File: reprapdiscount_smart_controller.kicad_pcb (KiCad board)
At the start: 2 copper layers, 150 x 55 mm, 38 parts, among them Q1 BC817, Q2 BC817, U1 74HC4050, U2 AMS1117-3.3

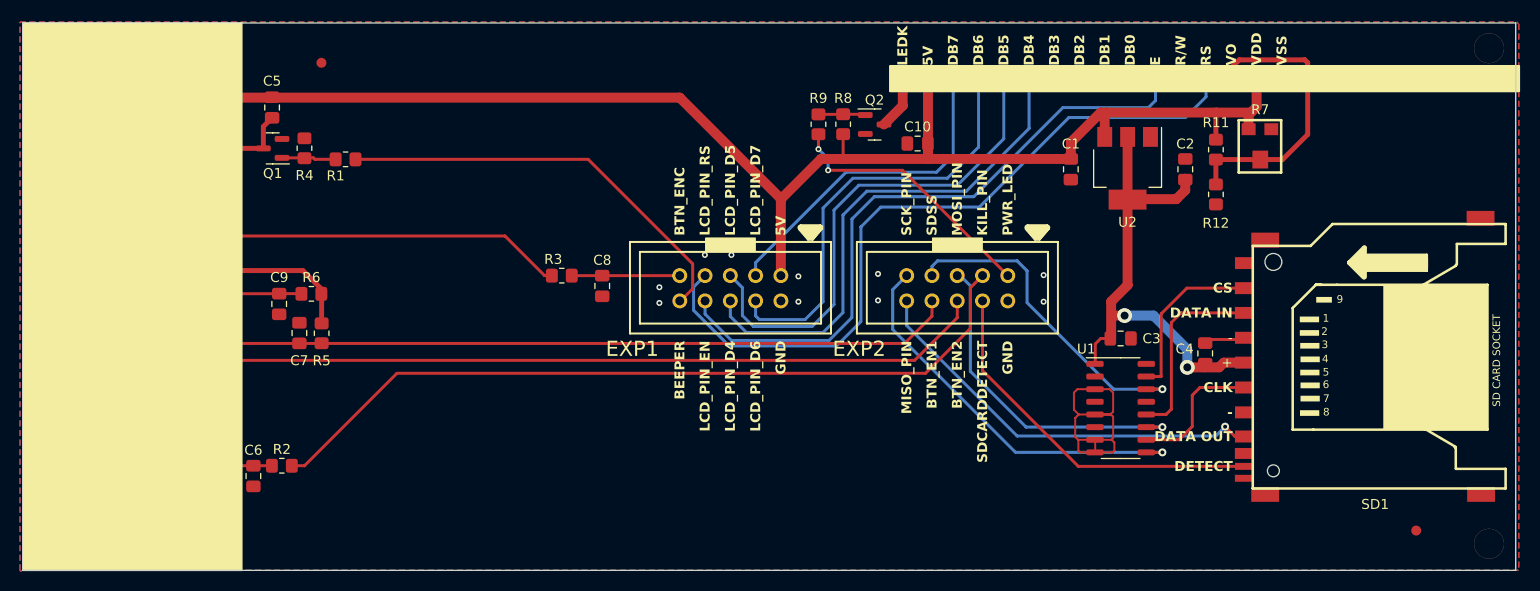
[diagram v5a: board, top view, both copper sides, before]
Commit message: feature: add back side fiducials
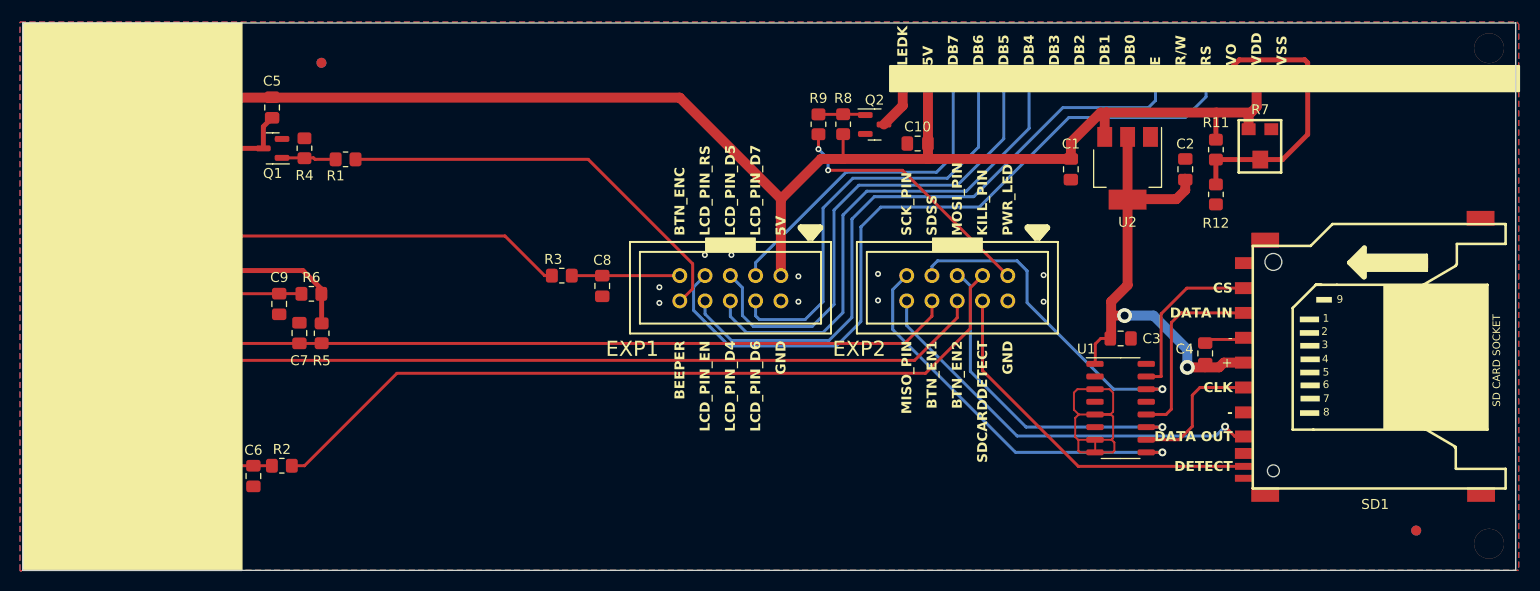
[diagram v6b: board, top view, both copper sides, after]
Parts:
- added FID3: Fiducial, Fiducial:Fiducial_1mm_Mask2mm, B.Cu at (213.5, 128.5)
- added FID4: Fiducial, Fiducial:Fiducial_1mm_Mask2mm, B.Cu at (103.5, 81.5)
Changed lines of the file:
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@@
     )
+  )
+  (footprint "Fiducial:Fiducial_1mm_Mask2mm" (layer "B.Cu")
+    (at 213.5011 128.5036 180)
+    (descr "Circular Fiducial, 1mm bare copper, 2mm soldermask opening (Level A)")
+    (tags "fiducial")
+    (property "Sheetfile" "reprapdiscount_smart_controller.kicad_sch")
+    (property "Sheetname" "")
+    (property "ki_description" "Fiducial Marker")
+    (property "ki_keywords" "fiducial marker")
+    (attr smd)
+    (fp_text reference "FID3" (at 0 2) (layer "B.Fab")
+        (effects (font (size 1 1) (thickness 0.15)) (justify mirror))
+    )
+    (fp_text value "Fiducial" (at 0 -2) (layer "B.Fab")
+        (effects (font (size 1 1) (thickness 0.15)) (justify mirror))
+    )
+    (fp_text user "${REFERENCE}" (at 0 0) (layer "B.Fab")
+        (effects (font (size 0.4 0.4) (thickness 0.06)) (justify mirror))
+    )
+    (fp_circle (center 0 0) (end 1.25 0)
+      (stroke (width 0.05) (type solid)) (fill none) (layer "B.CrtYd"))
+    (fp_circle (center 0 0) (end 1 0)
+      (stroke (width 0.1) (type solid)) (fill none) (layer "B.Fab"))
+    (pad "" smd circle (at 0 0 180) (size 1 1) (layers "B.Cu" "B.Mask")
+      (solder_mask_margin 0.5) (clearance 0.5))
+  )
+  (footprint "Fiducial:Fiducial_1mm_Mask2mm" (layer "B.Cu")
+    (at 103.5011 81.5036 180)
+    (descr "Circular Fiducial, 1mm bare copper, 2mm soldermask opening (Level A)")
+    (tags "fiducial")
+    (property "Sheetfile" "reprapdiscount_smart_controller.kicad_sch")
+    (property "Sheetname" "")
+    (property "ki_description" "Fiducial Marker")
+    (property "ki_keywords" "fiducial marker")
+    (attr smd)
+    (fp_text reference "FID4" (at 0 2) (layer "F.Fab")
+        (effects (font (size 1 1) (thickness 0.15)) (justify mirror))
+    )
+    (fp_text value "Fiducial" (at 0 -2) (layer "B.Fab")
+        (effects (font (size 1 1) (thickness 0.15)) (justify mirror))
+    )
+    (fp_text user "${REFERENCE}" (at 0 0) (layer "B.Fab")
+        (effects (font (size 0.4 0.4) (thickness 0.06)) (justify mirror))
+    )
+    (fp_circle (center 0 0) (end 1.25 0)
+      (stroke (width 0.05) (type solid)) (fill none) (layer "B.CrtYd"))
+    (fp_circle (center 0 0) (end 1 0)
+      (stroke (width 0.1) (type solid)) (fill none) (layer "B.Fab"))
+    (pad "" smd circle (at 0 0 180) (size 1 1) (layers "B.Cu" "B.Mask")
+      (solder_mask_margin 0.5) (clearance 0.5))
   )
   (footprint "reprapdiscount_smart_controller:PIEZO 11MM" (layer "B.Cu")

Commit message: feature: add stitching vias
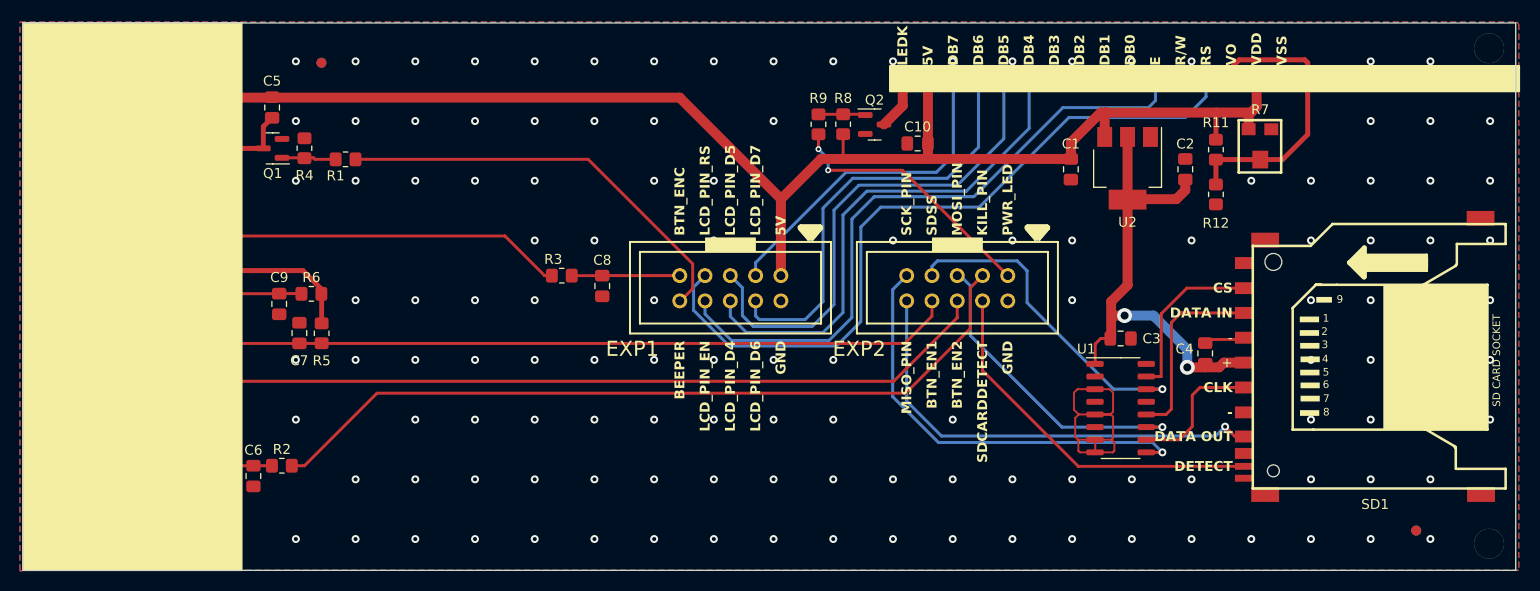
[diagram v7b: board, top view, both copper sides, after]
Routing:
- net /PB3_(MISO): track 41.8 -> 46.2 mm
- net /PB1_(SCK): track 39.9 -> 43.8 mm
- net /PB2_(MOSI): track 33.6 -> 31.5 mm
- net BTN_EN1: track 93.7 -> 95.5 mm
- net GND: vias 11 -> 147

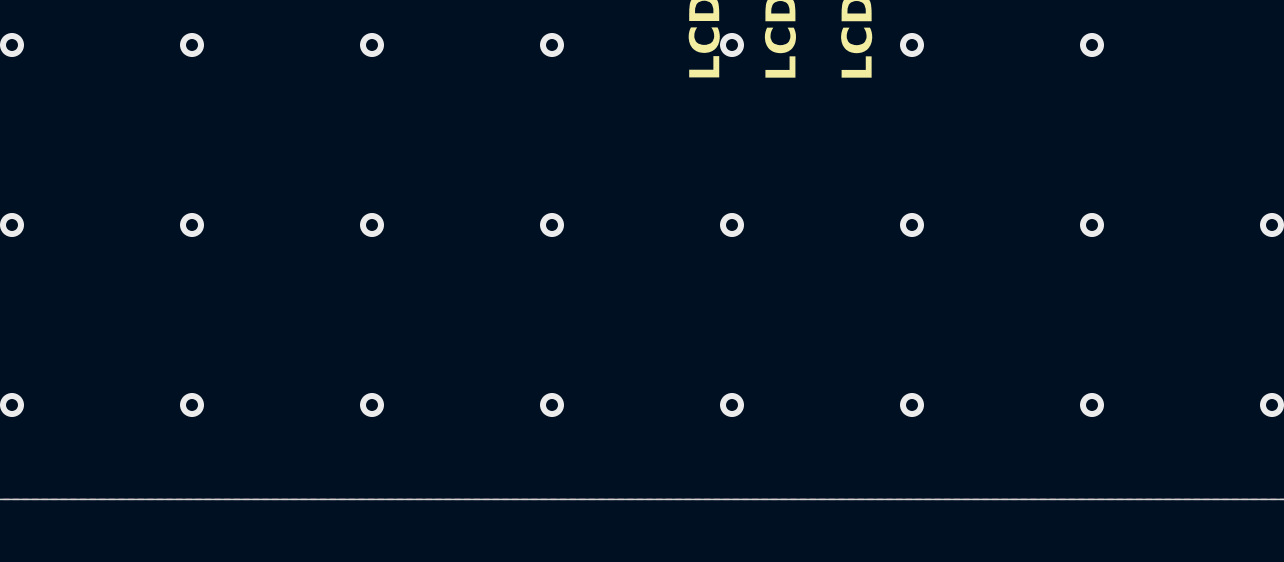
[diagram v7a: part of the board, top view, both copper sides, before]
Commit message: feature: add revision info to builds
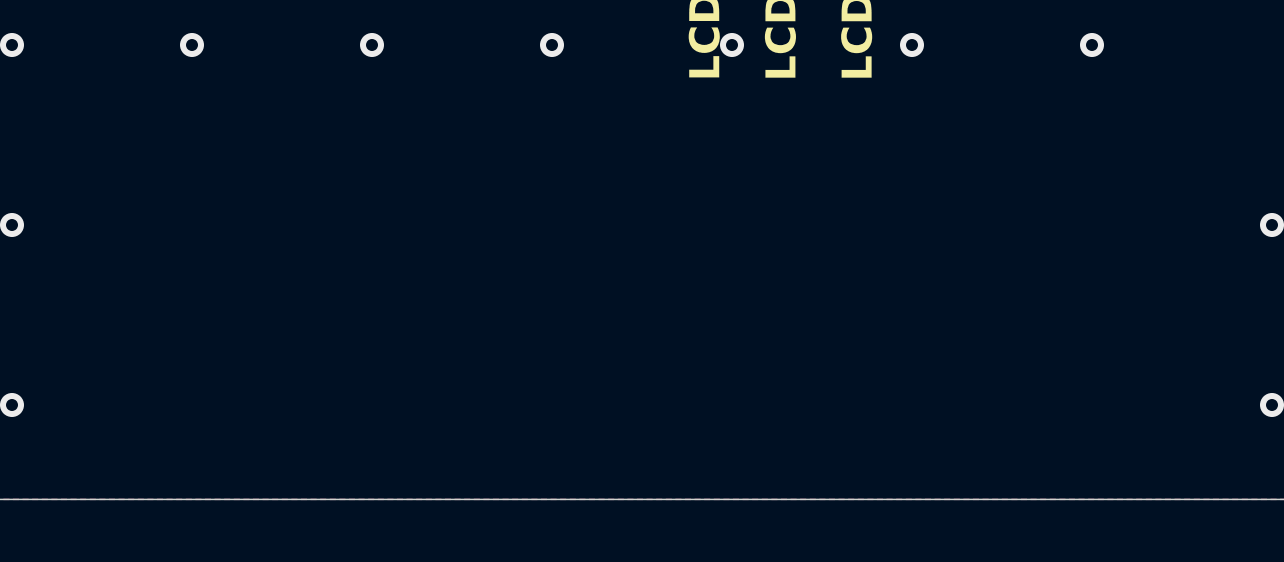
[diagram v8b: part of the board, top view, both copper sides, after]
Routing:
- net GND: vias 147 -> 135
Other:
- board text added: "RepRapDiscount Compatible Smart Controller Revision: ${TAG} (${REVISION}) Date: ${DATE}"
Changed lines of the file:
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@@
     )
   )
+  (property "DATE" "YYYY-MM-DD HH:MM:SS")
+  (property "REVISION" "REVISION")
+  (property "TAG" "TAG")
   (net 0 "")
   (net 1 "Net-(LCD1-Vo)")
@@
     (effects (font (size 1 1) (thickness 0.15) bold) (justify left))
   )
+  (gr_text "RepRapDiscount Compatible \nSmart Controller\nRevision: ${TAG} (${REVISION})\nDate: ${DATE}\n" (at 122.1511 125.1036) (layer "F.Mask")
+    (effects (font (size 1.5 1.5) (thickness 0.3) bold) (justify left))
+  )
   (gr_text "VDD" (at 204.9618 111.55235) (layer "User.1")
     (effects (font (size 0.762 0.762) (thickness 0.127)) (justify left bottom))
@@
   (via (at 94.92979 123.35611) (size 0.8) (drill 0.4) (layers "F.Cu" "B.Cu") (free) (net 6))
   (via (at 94.92979 129.35611) (size 0.8) (drill 0.4) (layers "F.Cu" "B.Cu") (free) (net 6))
-  (via (at 130.92979 123.35611) (size 0.8) (drill 0.4) (layers "F.Cu" "B.Cu") (free) (net 6))
   (via (at 82.92979 129.35611) (size 0.8) (drill 0.4) (layers "F.Cu" "B.Cu") (free) (net 6))
   (via (at 106.92979 123.35611) (size 0.8) (drill 0.4) (layers "F.Cu" "B.Cu") (free) (net 6))
-  (via (at 148.92979 123.35611) (size 0.8) (drill 0.4) (layers "F.Cu" "B.Cu") (free) (net 6))
   (via (at 178.92979 105.35611) (size 0.8) (drill 0.4) (layers "F.Cu" "B.Cu") (free) (net 6))
   (via (at 166.92979 117.35611) (size 0.8) (drill 0.4) (layers "F.Cu" "B.Cu") (free) (net 6))
@@
   (via (at 100.92979 87.35611) (size 0.8) (drill 0.4) (layers "F.Cu" "B.Cu") (free) (net 6))
   (via (at 88.92979 93.35611) (size 0.8) (drill 0.4) (layers "F.Cu" "B.Cu") (free) (net 6))
-  (via (at 142.92979 129.35611) (size 0.8) (drill 0.4) (layers "F.Cu" "B.Cu") (free) (net 6))
   (via (at 190.92979 123.35611) (size 0.8) (drill 0.4) (layers "F.Cu" "B.Cu") (free) (net 6))
-  (via (at 142.92979 123.35611) (size 0.8) (drill 0.4) (layers "F.Cu" "B.Cu") (free) (net 6))
-  (via (at 148.92979 129.35611) (size 0.8) (drill 0.4) (layers "F.Cu" "B.Cu") (free) (net 6))
   (via (at 220.92979 99.35611) (size 0.8) (drill 0.4) (layers "F.Cu" "B.Cu") (free) (net 6))
   (via (at 100.92979 129.35611) (size 0.8) (drill 0.4) (layers "F.Cu" "B.Cu") (free) (net 6))
@@
   (via (at 142.92979 99.35611) (size 0.8) (drill 0.4) (layers "F.Cu" "B.Cu") (free) (net 6))
   (via (at 148.92979 87.35611) (size 0.8) (drill 0.4) (layers "F.Cu" "B.Cu") (free) (net 6))
-  (via (at 136.92979 129.35611) (size 0.8) (drill 0.4) (layers "F.Cu" "B.Cu") (free) (net 6))
   (via (at 100.92979 93.35611) (size 0.8) (drill 0.4) (layers "F.Cu" "B.Cu") (free) (net 6))
   (via (at 112.92979 81.35611) (size 0.8) (drill 0.4) (layers "F.Cu" "B.Cu") (free) (net 6))
@@
   (via (at 124.92979 87.35611) (size 0.8) (drill 0.4) (layers "F.Cu" "B.Cu") (free) (net 6))
   (via (at 184.92979 81.35611) (size 0.8) (drill 0.4) (layers "F.Cu" "B.Cu") (free) (net 6))
-  (via (at 124.92979 129.35611) (size 0.8) (drill 0.4) (layers "F.Cu" "B.Cu") (free) (net 6))
   (via (at 202.92979 111.35611) (size 0.8) (drill 0.4) (layers "F.Cu" "B.Cu") (free) (net 6))
   (via (at 208.92979 117.35611) (size 0.8) (drill 0.4) (layers "F.Cu" "B.Cu") (free) (net 6))
@@
   (via (at 178.92979 123.35611) (size 0.8) (drill 0.4) (layers "F.Cu" "B.Cu") (free) (net 6))
   (via (at 148.92979 117.35611) (size 0.8) (drill 0.4) (layers "F.Cu" "B.Cu") (free) (net 6))
-  (via (at 154.92979 129.35611) (size 0.8) (drill 0.4) (layers "F.Cu" "B.Cu") (free) (net 6))
   (via (at 154.92979 111.35611) (size 0.8) (drill 0.4) (layers "F.Cu" "B.Cu") (free) (net 6))
-  (via (at 136.92979 123.35611) (size 0.8) (drill 0.4) (layers "F.Cu" "B.Cu") (free) (net 6))
   (via (at 142.92979 93.35611) (size 0.8) (drill 0.4) (layers "F.Cu" "B.Cu") (free) (net 6))
   (via (at 88.92979 117.35611) (size 0.8) (drill 0.4) (layers "F.Cu" "B.Cu") (free) (net 6))
@@
   (via (at 106.92979 111.35611) (size 0.8) (drill 0.4) (layers "F.Cu" "B.Cu") (free) (net 6))
   (via (at 100.92979 111.35611) (size 0.8) (drill 0.4) (layers "F.Cu" "B.Cu") (free) (net 6))
-  (via (at 130.92979 129.35611) (size 0.8) (drill 0.4) (layers "F.Cu" "B.Cu") (free) (net 6))
   (via (at 88.92979 129.35611) (size 0.8) (drill 0.4) (layers "F.Cu" "B.Cu") (free) (net 6))
   (via (at 106.92979 81.35611) (size 0.8) (drill 0.4) (layers "F.Cu" "B.Cu") (free) (net 6))
@@
   (via (at 124.92979 117.35611) (size 0.8) (drill 0.4) (layers "F.Cu" "B.Cu") (free) (net 6))
   (via (at 82.92979 117.35611) (size 0.8) (drill 0.4) (layers "F.Cu" "B.Cu") (free) (net 6))
-  (via (at 124.92979 123.35611) (size 0.8) (drill 0.4) (layers "F.Cu" "B.Cu") (free) (net 6))
   (via (at 190.92979 81.35611) (size 0.8) (drill 0.4) (layers "F.Cu" "B.Cu") (free) (net 6))
   (via (at 220.92979 93.35611) (size 0.8) (drill 0.4) (layers "F.Cu" "B.Cu") (free) (net 6))
@@
   (via (at 136.92979 117.35611) (size 0.8) (drill 0.4) (layers "F.Cu" "B.Cu") (free) (net 6))
   (via (at 160.92979 123.35611) (size 0.8) (drill 0.4) (layers "F.Cu" "B.Cu") (free) (net 6))
-  (via (at 154.92979 123.35611) (size 0.8) (drill 0.4) (layers "F.Cu" "B.Cu") (free) (net 6))
   (segment (start 167.38494 107.11976) (end 167.38494 105.42695) (width 0.3) (layer "F.Cu") (net 8))
   (segment (start 92.3011 105.1036) (end 92.3011 110.6036) (width 0.3) (layer "F.Cu") (net 8))
@@
       01bc2117-da22-446d-9df0-6c5cea9a90a2
       01cb03f0-40df-4d4c-8023-1dbffb4cdbf7
-      040aa517-3002-49ad-aaa6-d0d481a091e9
       06706409-adf1-4284-a4cc-4a6bb95c4c97
       0765d1c1-3ece-4d7c-9e65-39e9f63b977c
-      0a7abcca-be7e-4e7d-9afc-381b0e93788b
       0d1d2688-95ab-471d-ac54-3fb4efe1ee74
       1308b807-741a-4f7e-a990-287ce634dfae
@@
       32a72315-ec03-4a57-bbba-88c86973bb4a
       33a4b2f6-bca7-4743-a70c-33356c523c97
-      3515e69f-fa64-47bc-8366-1c5e674d8b97
       36e295ee-142d-48eb-9c08-eaaf97d4423c
-      3b0598ca-3a4b-4890-bc2d-7d7180c491d4
-      3d3bd8eb-0c8b-427c-968c-9b9d22f59677
       3df1e44d-a32e-4c61-9346-592f054bf848
       3f66dc68-71d5-4d8b-9528-064c7ab4a13e
@@
       6219bbd8-f9a3-4e57-b8a7-1ae84e564152
       625a614c-f821-4d10-b5d8-d801a7bea59a
-      6513fba1-0166-4af1-9002-8d301aa21216
       68f4fe87-0266-482b-b311-832d8d2bd5a4
       6920ba4a-6efc-4591-8b5a-9ce1ac233a14
@@
       a7334fe5-c514-455a-800b-68902e96c3f8
       a8b77383-159b-46b0-825f-a52df4a29b0e
-      a8d9dc2c-1501-43f1-a6a7-e28022db2782
       ac6d886b-caa2-48e8-89a2-5cde7a338632
       aea6088d-11c0-4fb3-b720-11efcb02a7e7
@@
       b2075d5b-5d55-4d6d-adc0-8a50118a6f04
       b2dd8ddc-dca0-4e25-ac74-b767444f6b5c
-      b3fe7866-779c-42d4-8843-69ef7cd0b007
       b44e333f-172c-41db-a1ea-a96749a7d8ee
-      b5530cb0-8823-462b-a5f6-a6ee0e0ea136
       b593236e-bcda-4752-a16a-f203a9e5fb28
       ba42e704-b831-4af0-8f9c-d0d5433a87ee
@@
       d4741a46-4b38-455e-99ce-5f8165d442e7
       d53b950c-f473-472d-ae20-e1597b30369b
-      d641b0dd-0c61-40c1-abd8-4d671e28f3ae
       d7027a8d-5d26-4173-ae8a-d2aff3a77351
       d7153cc8-04d3-4f28-ab5c-6c0f59f69912
@@
       dca88f2a-7649-497b-8981-c6959f7322a1
       e259ac56-e6fd-4bc7-bbbc-58dc73bbbd4e
-      e2be824a-b94d-46e1-8ae0-587173cf17ba
       e2f1872a-15ea-4ca2-8291-dee20ec6c5d1
       ecb1e058-c541-41e2-8abc-6ccbc45052a9
@@
       f4b3ee66-c534-4cfd-9681-770813fcb4ba
       f74b6eb9-8e23-4694-a631-8c1a8fd769df
-      fe58379d-bd44-4609-9b21-651e72af85f5
     )
   )
